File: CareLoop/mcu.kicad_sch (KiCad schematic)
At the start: 26 parts, among them J1_DEBUG1 Conn_01x04_Pin, U6 nRF52840-QFXX, Y1 32MHz, Y2 32.768kHz

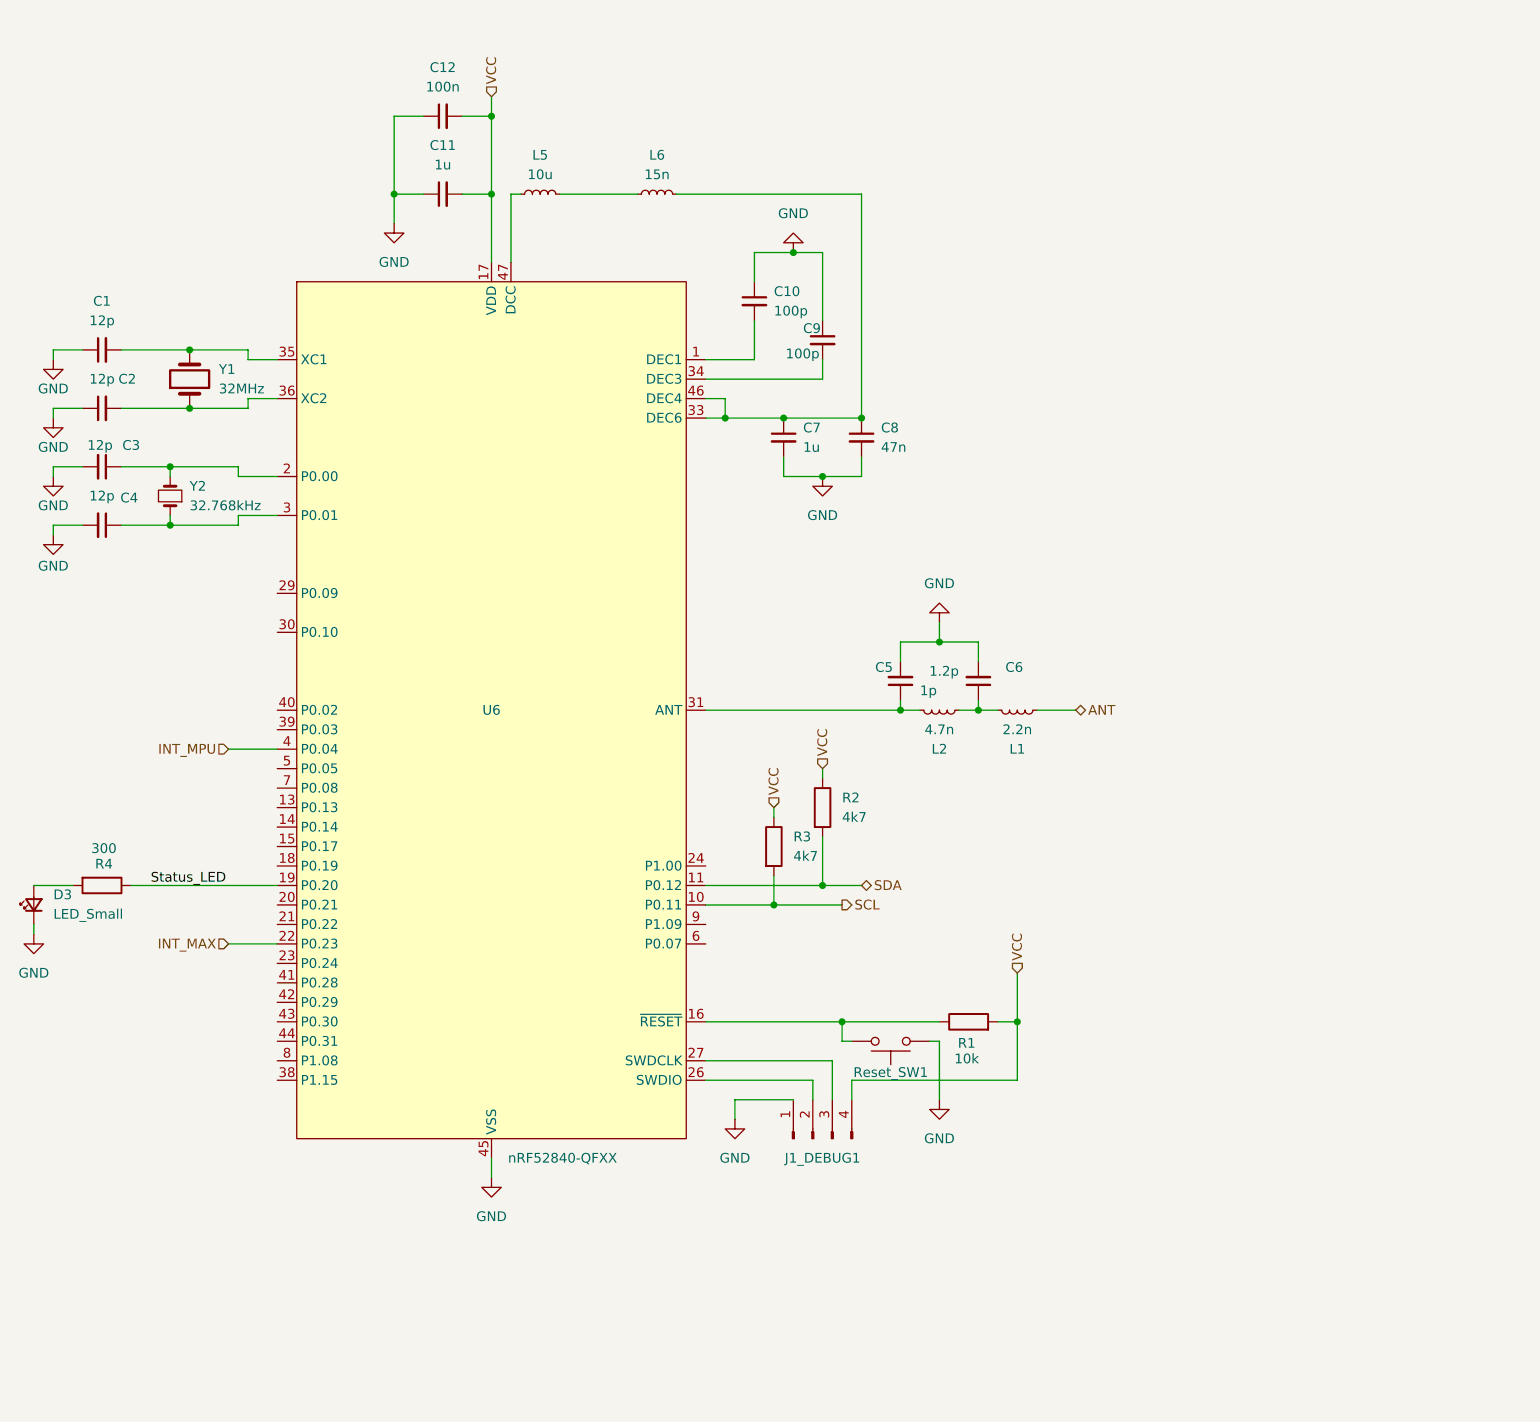
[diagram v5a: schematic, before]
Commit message: updated vias
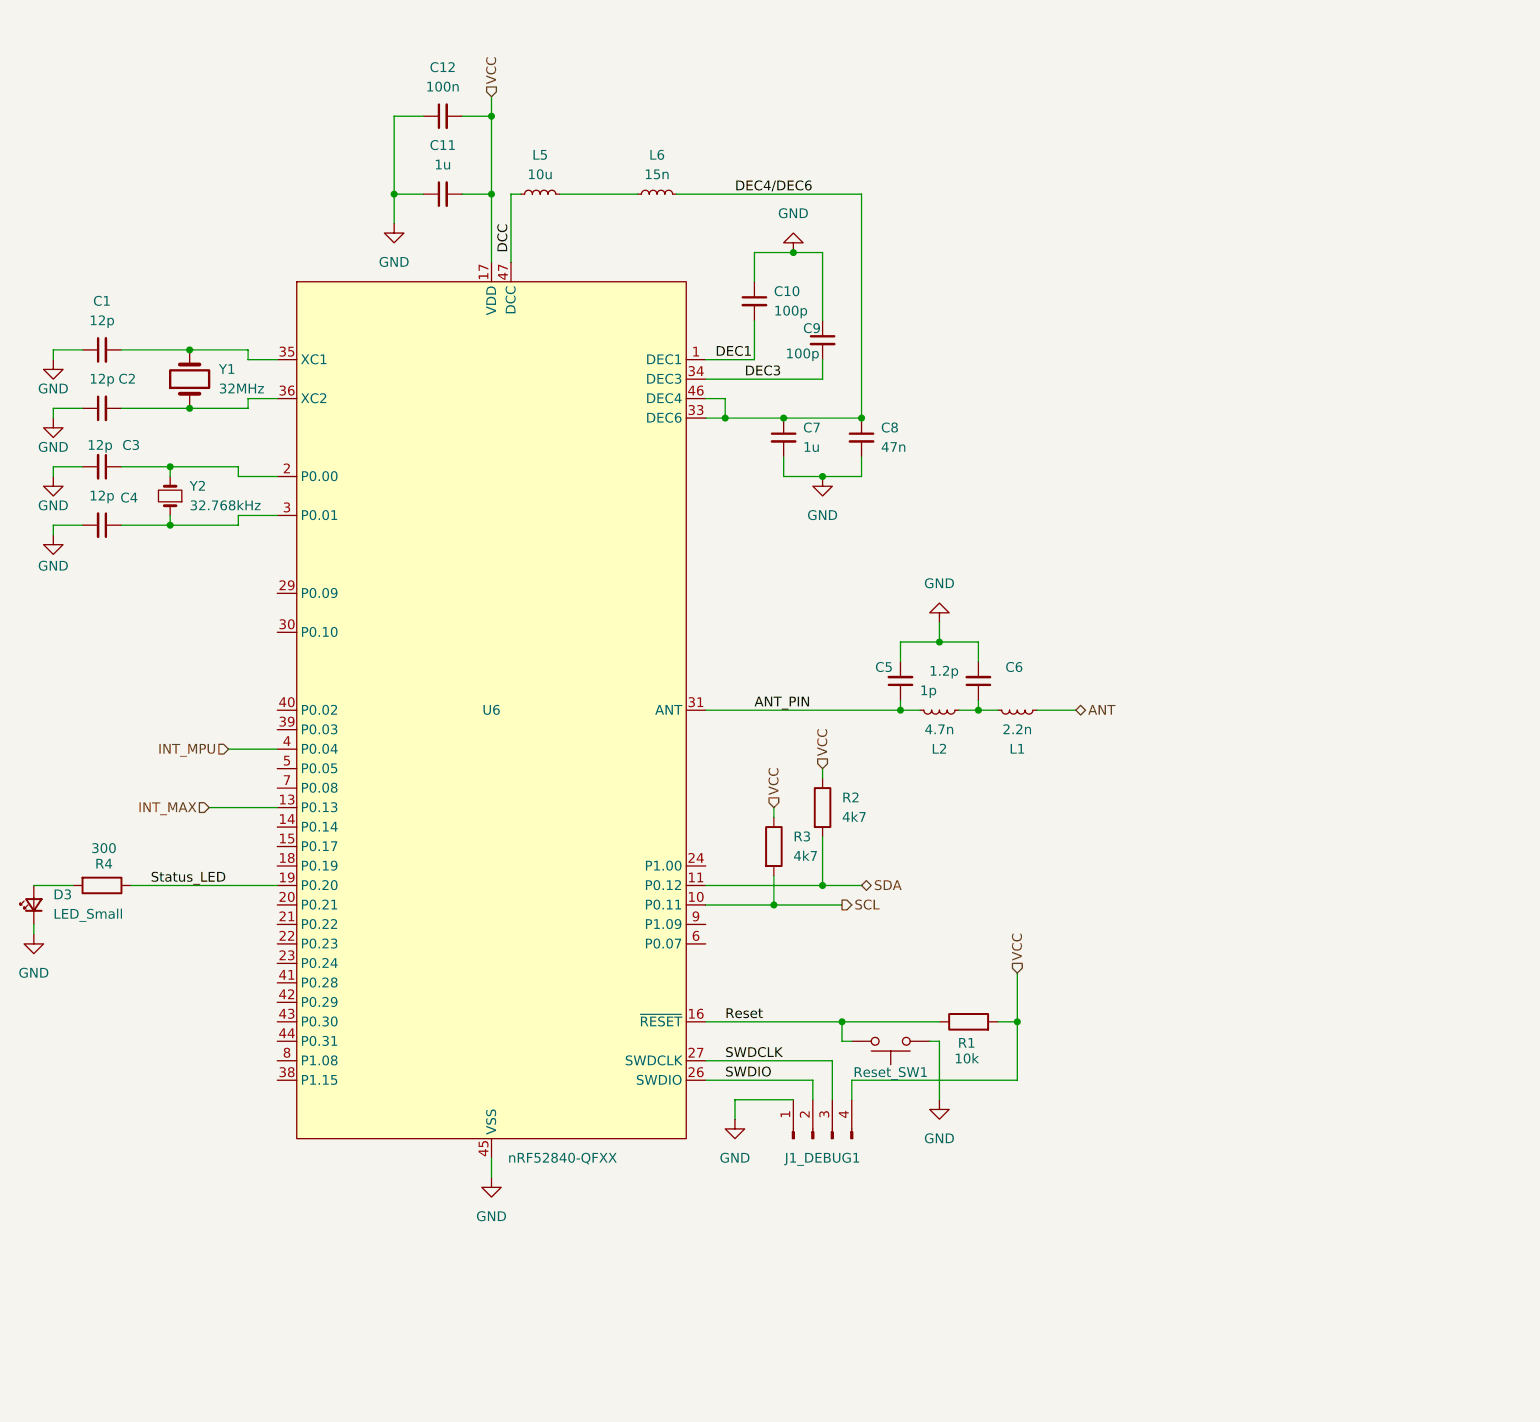
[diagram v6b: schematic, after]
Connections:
- net INT_MAX: now also U6.13 (P0.13); no longer U6.22 (P0.23)
- net DEC1: now reaches C10.2, U6.1 (DEC1)
- net Reset: now reaches R1.1, Reset_SW1.1, U6.16 (~{RESET})
- net SWDIO: now reaches J1_DEBUG1.2 (Pin_2), U6.26 (SWDIO)
- net SWDCLK: now reaches J1_DEBUG1.3 (Pin_3), U6.27 (SWDCLK)
- net ANT_PIN: now reaches C5.1, L2.2, U6.31 (ANT)
- net DEC4/DEC6: now reaches C7.1, C8.1, L6.2, U6.33 (DEC6), U6.46 (DEC4)
- net DEC3: now reaches C9.2, U6.34 (DEC3)
- net DCC: now reaches L5.1, U6.47 (DCC)
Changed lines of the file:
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@@
-	(wire
-		(pts
-			(xy 62.23 134.62) (xy 68.58 134.62)
-		)
-		(stroke
-			(width 0)
-			(type default)
-		)
-	)
 	(wire
 		(pts
@@
 	(wire
 		(pts
+			(xy 59.69 116.84) (xy 68.58 116.84)
+		)
+		(stroke
+			(width 0)
+			(type default)
+		)
+	)
+	(wire
+		(pts
 			(xy 139.7 60.96) (xy 139.7 58.42)
 		)
@@
 			(width 0)
 			(type default)
+		)
+	)
+	(label "SWDCLK"
+		(at 127 149.86 0)
+		(effects
+			(font
+				(size 1.27 1.27)
+			)
+			(justify left bottom)
+		)
+	)
+	(label "DEC4{slash}DEC6"
+		(at 128.27 36.83 0)
+		(effects
+			(font
+				(size 1.27 1.27)
+			)
+			(justify left bottom)
+		)
+	)
+	(label "DEC3"
+		(at 129.54 60.96 0)
+		(effects
+			(font
+				(size 1.27 1.27)
+			)
+			(justify left bottom)
 		)
 	)
@@
 		)
 	)
+	(label "ANT_PIN"
+		(at 130.81 104.14 0)
+		(effects
+			(font
+				(size 1.27 1.27)
+			)
+			(justify left bottom)
+		)
+	)
+	(label "SWDIO"
+		(at 127 152.4 0)
+		(effects
+			(font
+				(size 1.27 1.27)
+			)
+			(justify left bottom)
+		)
+	)
+	(label "Reset"
+		(at 127 144.78 0)
+		(effects
+			(font
+				(size 1.27 1.27)
+			)
+			(justify left bottom)
+		)
+	)
+	(label "DCC"
+		(at 99.06 44.45 90)
+		(effects
+			(font
+				(size 1.27 1.27)
+			)
+			(justify left bottom)
+		)
+	)
+	(label "DEC1"
+		(at 125.73 58.42 0)
+		(effects
+			(font
+				(size 1.27 1.27)
+			)
+			(justify left bottom)
+		)
+	)
 	(hierarchical_label "INT_MAX"
 		(shape input)
-		(at 62.23 134.62 180)
-		(effects
-			(font
+		(at 59.69 116.84 180)
+		(effects
+			(font

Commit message: update PCB
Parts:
- L1, L2: footprint Inductor_SMD:L_0402_1005Metric_Pad0.77x0.64mm_HandSolder -> Inductor_SMD:L_0201_0603Metric_Pad0.64x0.40mm_HandSolder
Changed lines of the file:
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@@
 			)
 		)
-		(property "Footprint" "Inductor_SMD:L_0402_1005Metric_Pad0.77x0.64mm_HandSolder"
+		(property "Footprint" "Inductor_SMD:L_0201_0603Metric_Pad0.64x0.40mm_HandSolder"
 			(at 154.94 104.14 0)
 			(effects
@@
 			)
 		)
-		(property "Footprint" "Inductor_SMD:L_0402_1005Metric_Pad0.77x0.64mm_HandSolder"
+		(property "Footprint" "Inductor_SMD:L_0201_0603Metric_Pad0.64x0.40mm_HandSolder"
 			(at 165.1 104.14 0)
 			(effects
